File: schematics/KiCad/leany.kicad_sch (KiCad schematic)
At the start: 41 parts, among them J1 SWD, J2 SSD1306, J3 USB_C, Q1 DMG6601LVT-7, SW2 ZERO_BTN, SW3 HOLD_BTN, SW4 BOOT, U1 STM32F103C8Tx, U2 AP2112K-3.3, U3 LSM6DSO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

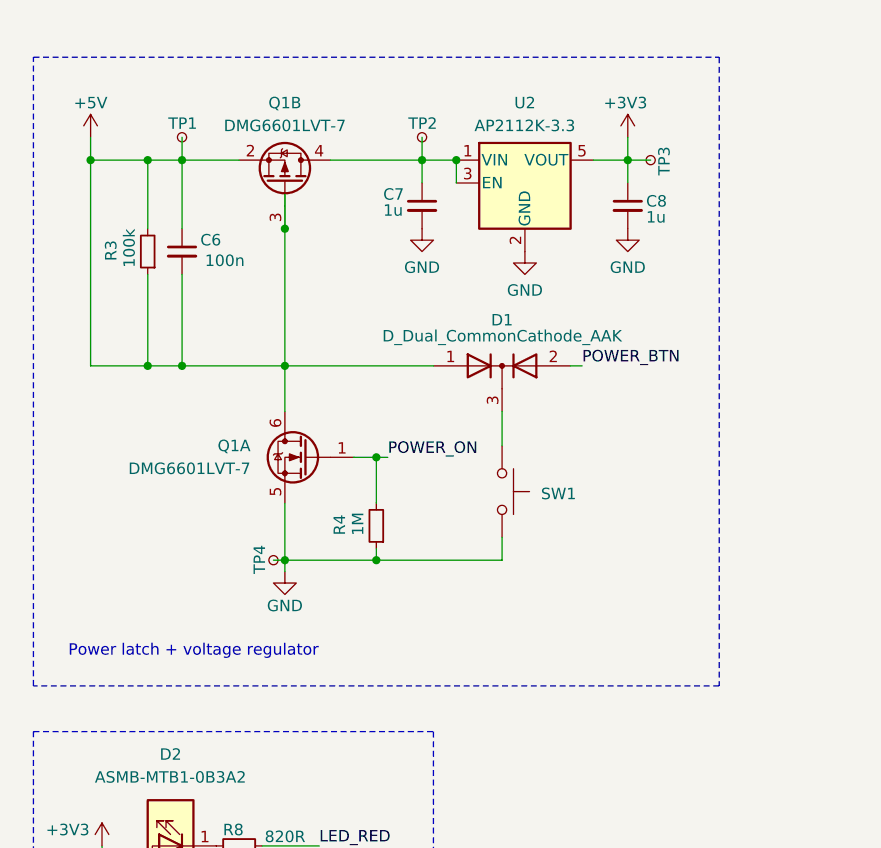
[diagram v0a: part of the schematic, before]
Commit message: fix power latch error
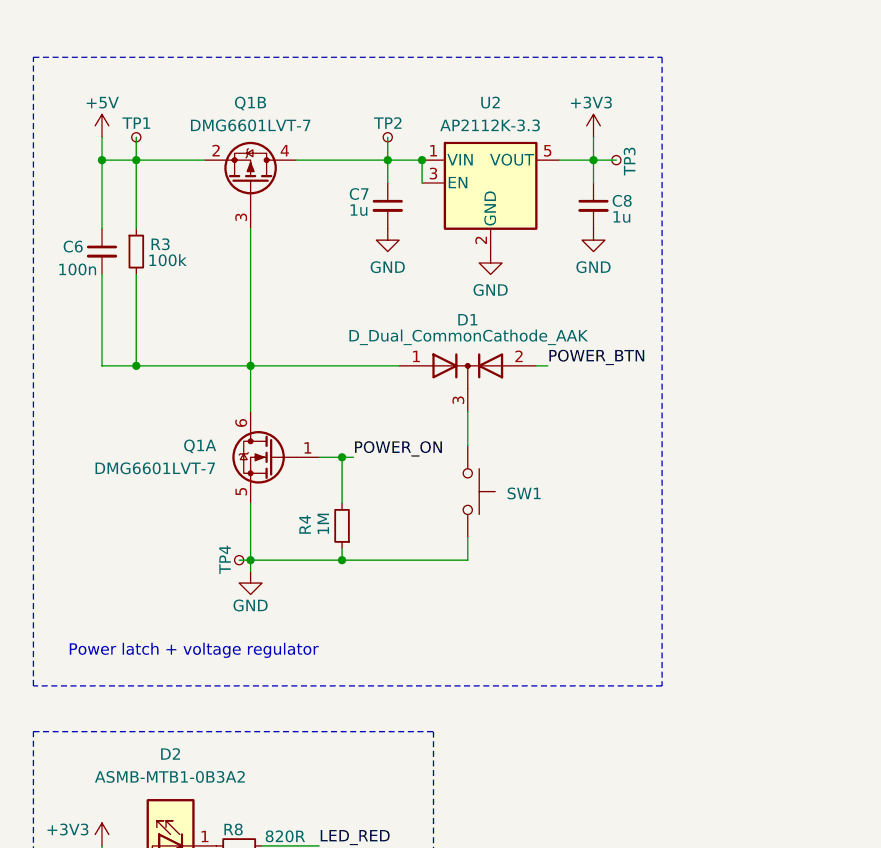
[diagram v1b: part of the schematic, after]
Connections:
- net +5V: no longer C6.2, D1.1 (A), Q1.3 (G), Q1.6 (D), R3.2
- new net: C6.2, D1.1 (A), Q1.3 (G), Q1.6 (D), R3.2
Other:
- moved on the sheet: C6, C7, C8, D1, Q1A, Q1B, R3, R4, SW1, TP1, TP2, TP3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

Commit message: disconnect FTDI reset
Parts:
- removed C12: 100nF, Capacitor_SMD:C_0201_0603Metric, symbol Device:C_Small
- removed R7: 10k, Resistor_SMD:R_0603_1608Metric, symbol Device:R_Small
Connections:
- net RESET is gone; now on net +3V3: U1.7 (NRST)
- no-connect marks 19 -> 20
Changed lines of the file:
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@@
 	)
 	(junction
-		(at 166.37 38.1)
-		(diameter 0)
-		(color 0 0 0 0)
-	)
-	(junction
 		(at 57.15 156.21)
 		(diameter 0)
@@
 	)
 	(no_connect
+		(at 86.36 171.45)
+	)
+	(no_connect
 		(at 167.64 83.82)
 	)
@@
 	(wire
 		(pts
-			(xy 163.83 38.1) (xy 166.37 38.1)
-		)
-		(stroke
-			(width 0)
-			(type default)
-		)
-	)
-	(wire
-		(pts
 			(xy 57.15 29.21) (xy 57.15 31.75)
 		)
@@
 	(wire
 		(pts
-			(xy 86.36 171.45) (xy 88.9 171.45)
-		)
-		(stroke
-			(width 0)
-			(type default)
-		)
-	)
-	(wire
-		(pts
 			(xy 162.56 99.06) (xy 167.64 99.06)
 		)
@@
 		)
 	)
-	(label "RESET"
-		(at 93.98 171.45 0)
-		(fields_autoplaced yes)
-		(effects
-			(font
-				(size 1.27 1.27)
-			)
-			(justify left bottom)
-		)
-	)
 	(label "LSM6DSO_SDO"
 		(at 229.87 129.54 180)
@@
 		)
 	)
-	(label "RESET"
-		(at 163.83 38.1 180)
-		(fields_autoplaced yes)
-		(effects
-			(font
-				(size 1.27 1.27)
-			)
-			(justify right bottom)
-		)
-	)
 	(label "FTDI_TX"
 		(at 88.9 156.21 0)
@@
 	(symbol
 		(lib_id "power:+3V3")
-		(at 166.37 30.48 0)
+		(at 166.37 35.56 0)
 		(unit 1)
 		(exclude_from_sim no)
@@
 		(dnp no)
 		(property "Reference" "#PWR016"
-			(at 166.37 34.29 0)
+			(at 166.37 39.37 0)
 			(effects
 				(font
@@
 		)
 		(property "Value" "+3V3"
-			(at 166.37 26.416 0)
+			(at 166.37 31.496 0)
 			(effects
 				(font
@@
 		)
 		(property "Footprint" ""
-			(at 166.37 30.48 0)
+			(at 166.37 35.56 0)
 			(effects
 				(font
@@
 		)
 		(property "Datasheet" ""
-			(at 166.37 30.48 0)
+			(at 166.37 35.56 0)
 			(effects
 				(font
@@
 		)
 		(property "Description" "Power symbol creates a global label with name \"+3V3\""
-			(at 166.37 30.48 0)
+			(at 166.37 35.56 0)
 			(effects
 				(font
@@
 	)
 	(symbol
-		(lib_id "Device:C_Small")
-		(at 91.44 171.45 90)
-		(unit 1)
-		(exclude_from_sim no)
-		(in_bom yes)
-		(on_board yes)
-		(dnp no)
-		(property "Reference" "C12"
-			(at 91.44 168.656 90)
-			(effects
-				(font
-					(size 1.27 1.27)
-				)
-			)
-		)
-		(property "Value" "100nF"
-			(at 91.948 166.624 90)
-			(effects
-				(font
-					(size 1.27 1.27)
-				)
-			)
-		)
-		(property "Footprint" "Capacitor_SMD:C_0201_0603Metric"
-			(at 91.44 171.45 0)
-			(effects
-				(font
-					(size 1.27 1.27)
-				)
-				(hide yes)
-			)
-		)
-		(property "Datasheet" "~"
-			(at 91.44 171.45 0)
-			(effects
-				(font
-					(size 1.27 1.27)
-				)
-				(hide yes)
-			)
-		)
-		(property "Description" "Unpolarized capacitor, small symbol"
-			(at 91.44 171.45 0)
-			(effects
-				(font
-					(size 1.27 1.27)
-				)
-				(hide yes)
-			)
-		)
-		(pin "2"
-		)
-		(pin "1"
-		)
-		(instances
-			(project "leany"
-				(path "/e47b2519-93ca-4a48-9414-ecc253dd35f5"
-					(reference "C12")
-					(unit 1)
-				)
-			)
-		)
-	)
-	(symbol
 		(lib_id "Device:R_Small")
 		(at 40.64 105.41 90)
@@
 					(unit 1)
 				)
-			)
-		)
-	)
-	(symbol
-		(lib_id "Device:R_Small")
-		(at 166.37 33.02 180)
-		(unit 1)
-		(exclude_from_sim no)
-		(in_bom yes)
-		(on_board yes)
-		(dnp no)
-		(property "Reference" "R7"
-			(at 168.402 30.734 90)
-			(effects
-				(font
-					(size 1.27 1.27)
-				)
-				(justify left)
-			)
-		)
-		(property "Value" "10k"
-			(at 170.18 29.464 90)
-			(effects
-				(font
-					(size 1.27 1.27)
-				)
-				(justify left)
-			)
-		)
-		(property "Footprint" "Resistor_SMD:R_0603_1608Metric"
-			(at 166.37 33.02 0)
-			(effects
-				(font
-					(size 1.27 1.27)
-				)
-				(hide yes)
-			)
-		)
-		(property "Datasheet" "~"
-			(at 166.37 33.02 0)
-			(effects
-				(font
-					(size 1.27 1.27)
-				)
-				(hide yes)
-			)
-		)
-		(property "Description" "Resistor, small symbol"
-			(at 166.37 33.02 0)
-			(effects
-				(font
-					(size 1.27 1.27)
-				)
-				(hide yes)
-			)
-		)
-		(pin "1"
-		)
-		(pin "2"
-		)
-		(instances
-			(project "leany"
-				(path "/e47b2519-93ca-4a48-9414-ecc253dd35f5"
-					(reference "R7")
-					(unit 1)
-				)

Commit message: rename bootmode switch
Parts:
- SW4: value BOOT -> BOOTMODE_SW
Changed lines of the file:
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@@
 	(title_block
 		(title "Leany")
-		(date "2024-08-26")
+		(date "2024-08-28")
 		(comment 1 "MIT License")
 		(comment 2 "Copyright (c) 2023 Gilles Henrard")
@@
 			)
 		)
-		(property "Value" "BOOT"
-			(at 144.526 28.956 0)
+		(property "Value" "BOOTMODE_SW"
+			(at 148.336 28.956 0)
 			(effects
 				(font

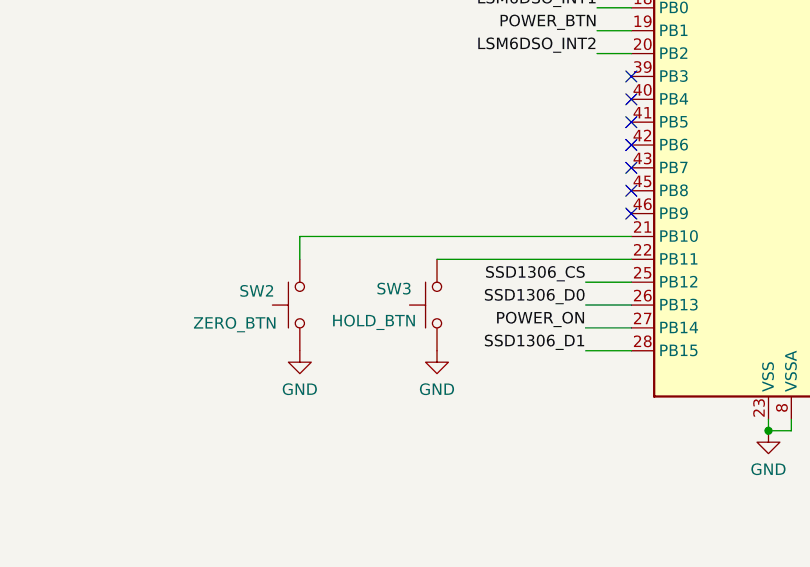
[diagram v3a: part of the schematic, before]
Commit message: reorganise zero and hold buttons
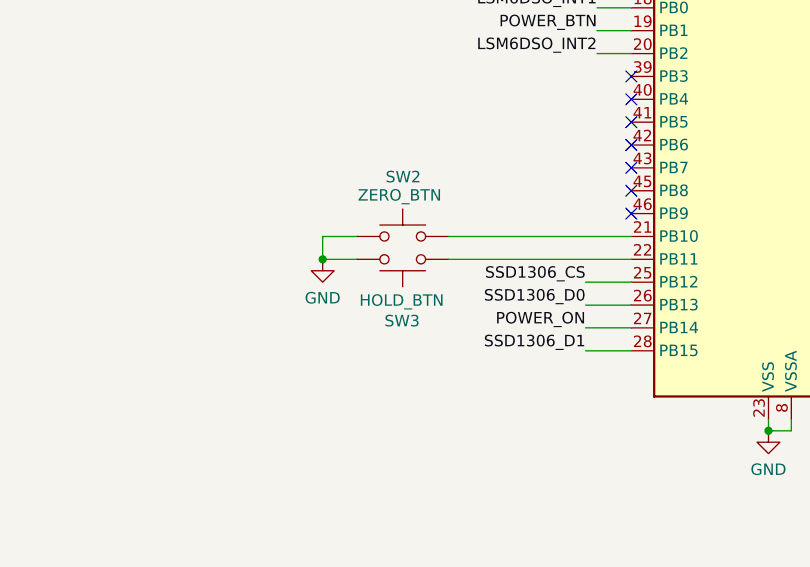
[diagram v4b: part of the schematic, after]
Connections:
- net GND: now also SW3.1; no longer SW3.2
- net at U1.22 (PB11): now also SW3.2; no longer SW3.1
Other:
- moved on the sheet: SW2, SW3
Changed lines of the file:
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@@
 	)
 	(junction
+		(at 133.35 93.98)
+		(diameter 0)
+		(color 0 0 0 0)
+	)
+	(junction
 		(at 57.15 156.21)
 		(diameter 0)
@@
 	(wire
 		(pts
+			(xy 133.35 91.44) (xy 133.35 93.98)
+		)
+		(stroke
+			(width 0)
+			(type default)
+		)
+	)
+	(wire
+		(pts
 			(xy 149.86 48.26) (xy 146.05 48.26)
 		)
@@
 	(wire
 		(pts
+			(xy 137.16 91.44) (xy 133.35 91.44)
+		)
+		(stroke
+			(width 0)
+			(type default)
+		)
+	)
+	(wire
+		(pts
 			(xy 254 109.22) (xy 254 110.49)
 		)
@@
 	(wire
 		(pts
-			(xy 130.81 91.44) (xy 167.64 91.44)
+			(xy 147.32 91.44) (xy 167.64 91.44)
 		)
 		(stroke
@@
 	(wire
 		(pts
-			(xy 146.05 93.98) (xy 167.64 93.98)
+			(xy 147.32 93.98) (xy 167.64 93.98)
 		)
 		(stroke
@@
 	(wire
 		(pts
+			(xy 133.35 93.98) (xy 137.16 93.98)
+		)
+		(stroke
+			(width 0)
+			(type default)
+		)
+	)
+	(wire
+		(pts
 			(xy 48.26 161.29) (xy 52.07 161.29)
 		)
@@
 	(wire
 		(pts
-			(xy 130.81 93.98) (xy 130.81 91.44)
-		)
-		(stroke
-			(width 0)
-			(type default)
-		)
-	)
-	(wire
-		(pts
 			(xy 200.66 60.96) (xy 203.2 60.96)
 		)
@@
 	)
 	(symbol
-		(lib_id "power:GND")
-		(at 130.81 104.14 0)
-		(unit 1)
-		(exclude_from_sim no)
-		(in_bom yes)
-		(on_board yes)
-		(dnp no)
-		(property "Reference" "#PWR023"
-			(at 130.81 110.49 0)
-			(effects
-				(font
-					(size 1.27 1.27)
-				)
-				(hide yes)
-			)
-		)
-		(property "Value" "GND"
-			(at 130.81 108.458 0)
-			(effects
-				(font
-					(size 1.27 1.27)
-				)
-			)
-		)
-		(property "Footprint" ""
-			(at 130.81 104.14 0)
-			(effects
-				(font
-					(size 1.27 1.27)
-				)
-				(hide yes)
-			)
-		)
-		(property "Datasheet" ""
-			(at 130.81 104.14 0)
-			(effects
-				(font
-					(size 1.27 1.27)
-				)
-				(hide yes)
-			)
-		)
-		(property "Description" "Power symbol creates a global label with name \"GND\" , ground"
-			(at 130.81 104.14 0)
-			(effects
-				(font
-					(size 1.27 1.27)
-				)
-				(hide yes)
-			)
-		)
-		(pin "1"
-		)
-		(instances
-			(project "leany"
-				(path "/e47b2519-93ca-4a48-9414-ecc253dd35f5"
-					(reference "#PWR023")
-					(unit 1)
-				)
-			)
-		)
-	)
-	(symbol
 		(lib_id "Device:C_Small")
 		(at 254 113.03 0)
@@
 	(symbol
 		(lib_id "power:GND")
-		(at 146.05 104.14 0)
+		(at 133.35 93.98 0)
 		(unit 1)
 		(exclude_from_sim no)
@@
 		(dnp no)
 		(property "Reference" "#PWR022"
-			(at 146.05 110.49 0)
+			(at 133.35 100.33 0)
 			(effects
 				(font
@@
 		)
 		(property "Value" "GND"
-			(at 146.05 108.458 0)
+			(at 133.35 98.298 0)
 			(effects
 				(font
@@
 		)
 		(property "Footprint" ""
-			(at 146.05 104.14 0)
+			(at 133.35 93.98 0)
 			(effects
 				(font
@@
 		)
 		(property "Datasheet" ""
-			(at 146.05 104.14 0)
+			(at 133.35 93.98 0)
 			(effects
 				(font
@@
 		)
 		(property "Description" "Power symbol creates a global label with name \"GND\" , ground"
-			(at 146.05 104.14 0)
+			(at 133.35 93.98 0)
 			(effects
 				(font
@@
 	(symbol
 		(lib_id "Switch:SW_Push")
-		(at 130.81 99.06 90)
-		(mirror x)
+		(at 142.24 91.44 0)
+		(mirror y)
 		(unit 1)
 		(exclude_from_sim no)
@@
 		(dnp no)
 		(property "Reference" "SW2"
-			(at 128.016 97.536 90)
+			(at 144.272 84.836 0)
 			(effects
 				(font
@@
 		)
 		(property "Value" "ZERO_BTN"
-			(at 128.27 101.092 90)
+			(at 146.558 86.868 0)
 			(effects
 				(font
@@
 		)
 		(property "Footprint" ""
-			(at 125.73 99.06 0)
+			(at 142.24 86.36 0)
 			(effects
 				(font
@@
 		)
 		(property "Datasheet" "~"
-			(at 125.73 99.06 0)
+			(at 142.24 86.36 0)
 			(effects
 				(font
@@
 		)
 		(property "Description" "Push button switch, generic, two pins"
-			(at 130.81 99.06 0)
+			(at 142.24 91.44 0)
 			(effects
 				(font
@@
 	(symbol
 		(lib_id "Switch:SW_Push")
-		(at 146.05 99.06 90)
+		(at 142.24 93.98 0)
 		(mirror x)
 		(unit 1)
@@
 		(dnp no)
 		(property "Reference" "SW3"
-			(at 143.256 97.282 90)
+			(at 140.208 100.838 0)
 			(effects
 				(font
@@
 		)
 		(property "Value" "HOLD_BTN"
-			(at 143.764 100.838 90)
+			(at 137.414 98.552 0)
 			(effects
 				(font
@@
 		)
 		(property "Footprint" ""
-			(at 140.97 99.06 0)
+			(at 142.24 99.06 0)
 			(effects
 				(font
@@
 		)
 		(property "Datasheet" "~"
-			(at 140.97 99.06 0)
+			(at 142.24 99.06 0)
 			(effects
 				(font
@@
 		)
 		(property "Description" "Push button switch, generic, two pins"
-			(at 146.05 99.06 0)
+			(at 142.24 93.98 0)
 			(effects
 				(font

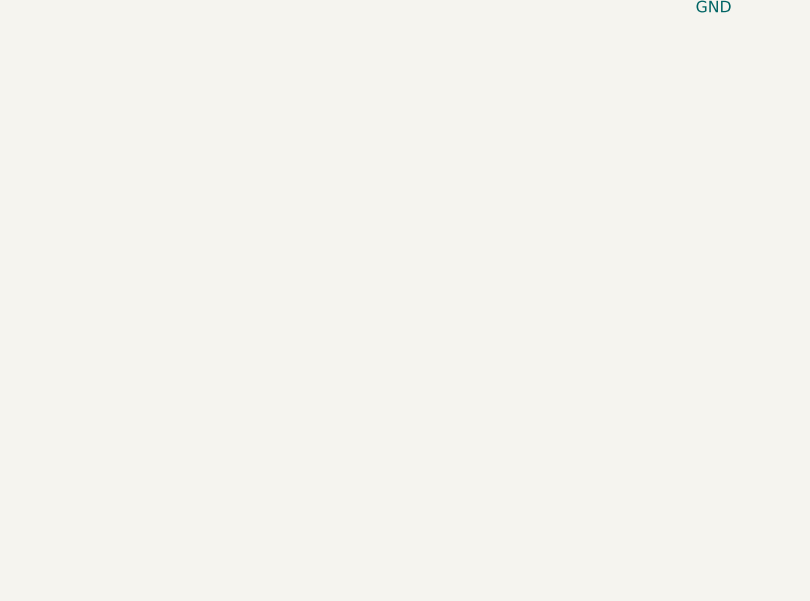
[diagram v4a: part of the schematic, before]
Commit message: create and place battery manager
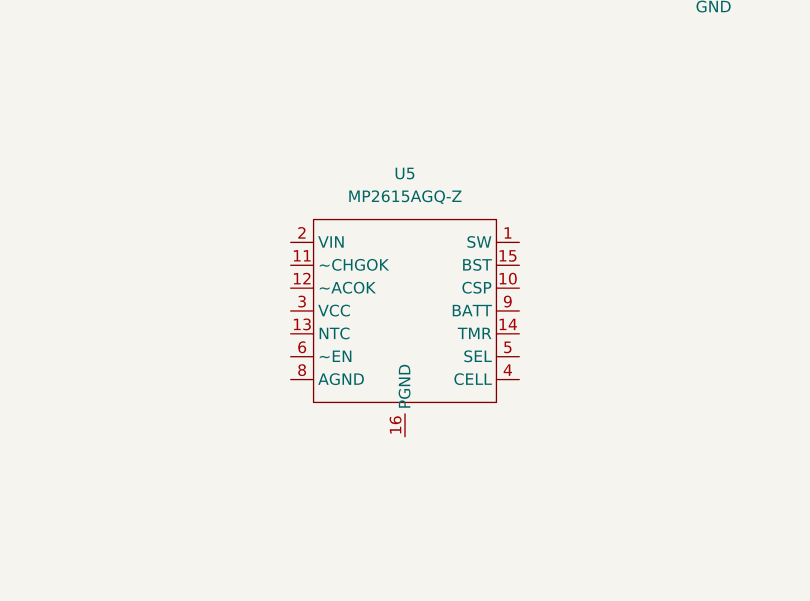
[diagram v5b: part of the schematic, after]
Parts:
- added U5: MP2615AGQ-Z, symbol leany-symbols:MP2615AGQ-Z
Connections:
- new net: U5.16 (PGND), U5.7 (NC)
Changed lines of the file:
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@@
+	)
+	(symbol
+		(lib_id "leany-symbols:MP2615AGQ-Z")
+		(at 148.59 151.13 0)
+		(unit 1)
+		(exclude_from_sim no)
+		(in_bom yes)
+		(on_board yes)
+		(dnp no)
+		(fields_autoplaced yes)
+		(property "Reference" "U5"
+			(at 148.59 135.89 0)
+			(effects
+				(font
+					(size 1.27 1.27)
+				)
+			)
+		)
+		(property "Value" "MP2615AGQ-Z"
+			(at 148.59 138.43 0)
+			(effects
+				(font
+					(size 1.27 1.27)
+				)
+			)
+		)
+		(property "Footprint" ""
+			(at 148.59 151.13 0)
+			(effects
+				(font
+					(size 1.27 1.27)
+				)
+				(hide yes)
+			)
+		)
+		(property "Datasheet" "https://www.monolithicpower.com/en/documentview/productdocument/index/version/2/document_type/Datasheet/lang/en/sku/MP2615GQ-Z/document_id/1423"
+			(at 148.59 151.13 0)
+			(effects
+				(font
+					(size 1.27 1.27)
+				)
+				(hide yes)
+			)
+		)
+		(property "Description" "2A, 1- CELL OR 2- CELL LI-ION BATTERY CHARGER"
+			(at 148.59 151.13 0)
+			(effects
+				(font
+					(size 1.27 1.27)
+				)
+				(hide yes)
+			)
+		)
+		(pin "4"
+		)
+		(pin "7"
+		)
+		(pin "9"
+		)
+		(pin "15"
+		)
+		(pin "10"
+		)
+		(pin "2"
+		)
+		(pin "1"
+		)
+		(pin "12"
+		)
+		(pin "14"
+		)
+		(pin "8"
+		)
+		(pin "13"
+		)
+		(pin "16"
+		)
+		(pin "6"
+		)
+		(pin "11"
+		)
+		(pin "3"
+		)
+		(pin "5"
+		)
+		(instances
+			(project ""
+				(path "/e47b2519-93ca-4a48-9414-ecc253dd35f5"
+					(reference "U5")
+					(unit 1)
+				)
+			)
+		)
 	)
 	(symbol
